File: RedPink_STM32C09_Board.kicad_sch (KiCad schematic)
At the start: 33 parts, among them IC1 STM32C092CBT6, IC3 ATA6561-GAQW-N, IC4 LDLN025M18R, IC5 FT231XS-U, J1 USB4216-03-A, J2 SWD DEBUG, J3 CANBUS, Y1 NX3225GD-8MHZ-STD-CRA-3

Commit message: Updated design - focus on CAN-USB Application
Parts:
- added FL1: DR221-513AE, RedPink_STM32C09_Board:DR221474AE, symbol RedPink_STM32C09_Board:DR221-513AE
- added H1, H2, H3, H4: MountingHole_Pad, MountingHole:MountingHole_2.5mm_Pad, symbol Mechanical:MountingHole_Pad
- JP1: footprint Connector_PinHeader_2.54mm:PinHeader_1x02_P2.54mm_Vertical -> Jumper:SolderJumper-2_P1.3mm_Open_RoundedPad1.0x1.5mm
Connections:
- net VBUS is gone; now on net 5V: FB1.1, IC5.15 (VCC)
- net 3V3: now also C12.1, C13.1, IC1.6 (VDD/VDDA), J2.4 (Pin_4), R6.2
- net CANH: now also FL1.4; no longer IC3.7 (CANH)
- net CANL: now also FL1.3; no longer IC3.6 (CANL)
- net GND: now also H1.1, H2.1, H3.1, H4.1
- net SWCLK: now also J2.2 (Pin_2); no longer J2.3 (Pin_3)
- net SWDIO: now also J2.3 (Pin_3); no longer J2.4 (Pin_4)
- net USBDP: now reaches IC5.11 (USBDP), R2.1
- net USBDN: now reaches IC5.12 (USBDM), R1.2
- removed net VDD: C12.1, C13.1, IC1.6 (VDD/VDDA), J2.2 (Pin_2), R6.2
- new net: FL1.2, IC3.6 (CANL)
- new net: FL1.1, IC3.7 (CANH)
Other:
- moved on the sheet: C10, C11, C14, C2, C3, C4, C5, C6, C9, D1, FB1, IC4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

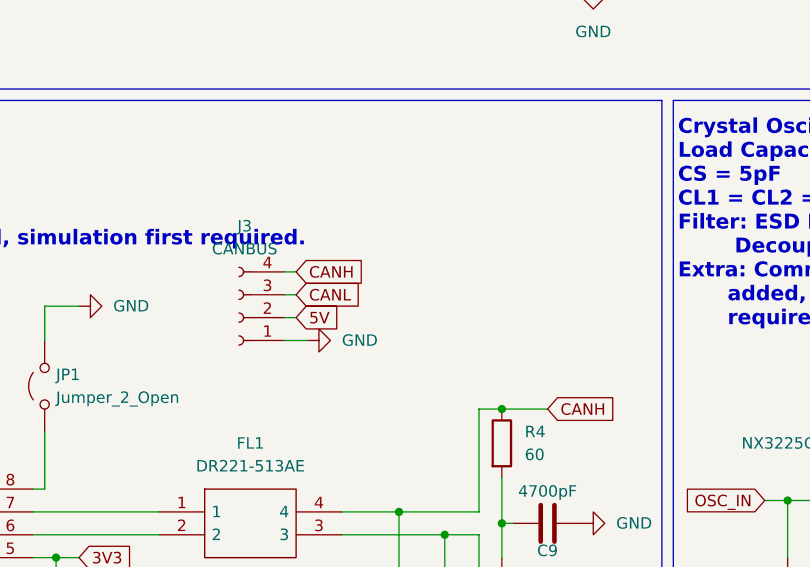
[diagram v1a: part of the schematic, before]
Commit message: Updated PCB layout, output connector replaced
1) Removed 5V pin from output pin header
2) Added round corners
3) Replace pin header output
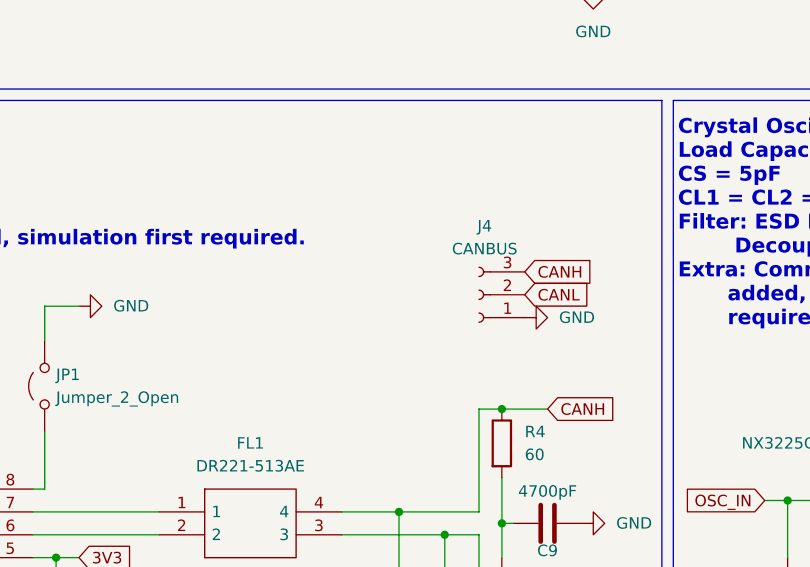
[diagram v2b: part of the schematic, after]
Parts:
- removed J3: CANBUS, Connector_PinHeader_2.54mm:PinHeader_1x04_P2.54mm_Vertical, symbol Connector:Conn_01x04_Socket
- added J4: CANBUS, Connector_PinHeader_2.54mm:PinHeader_1x03_P2.54mm_Vertical, symbol Connector:Conn_01x03_Socket
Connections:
- net CANH: now also J4.3 (Pin_3)
- net CANL: now also J4.2 (Pin_2)
- net GND: now also J4.1 (Pin_1)
